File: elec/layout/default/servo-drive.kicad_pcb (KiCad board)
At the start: 4 copper layers, 37.6 x 39.9 mm, 125 parts

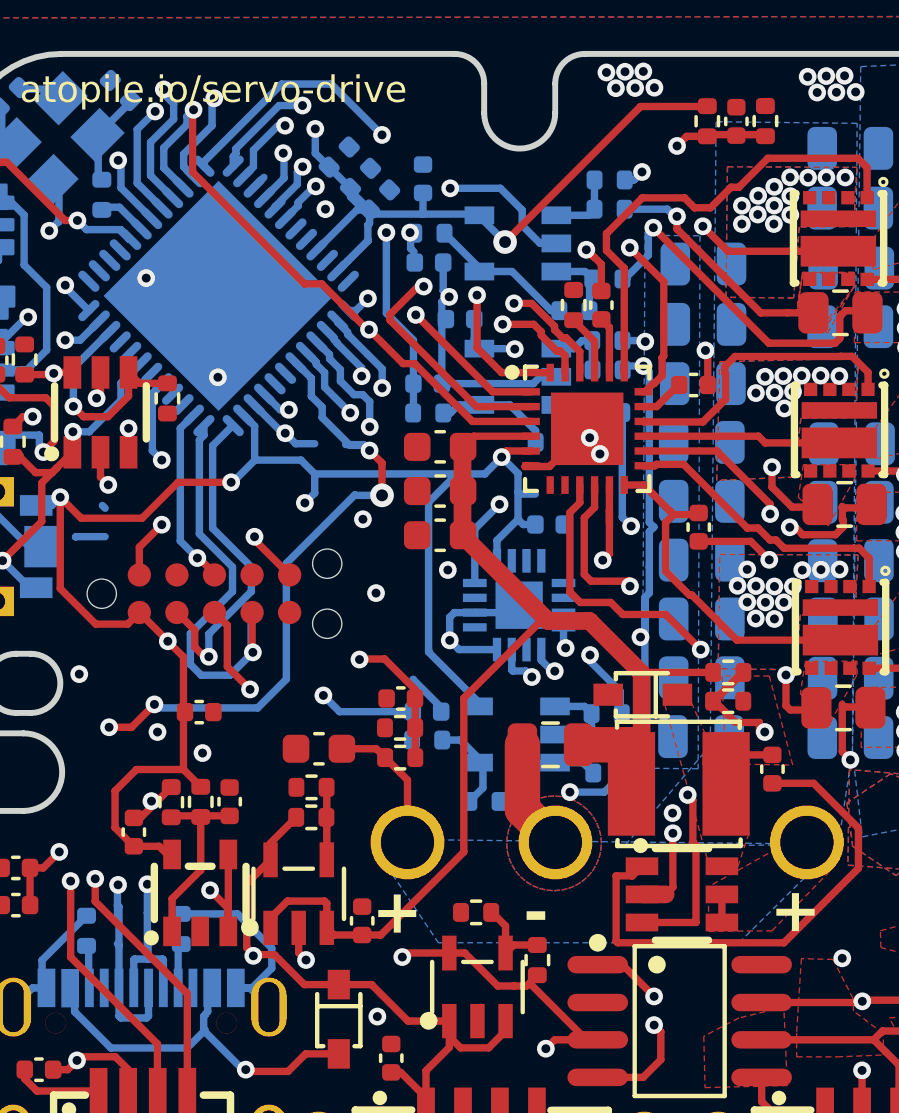
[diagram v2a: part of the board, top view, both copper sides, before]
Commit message: swapping MA732 for MT6835 sensor
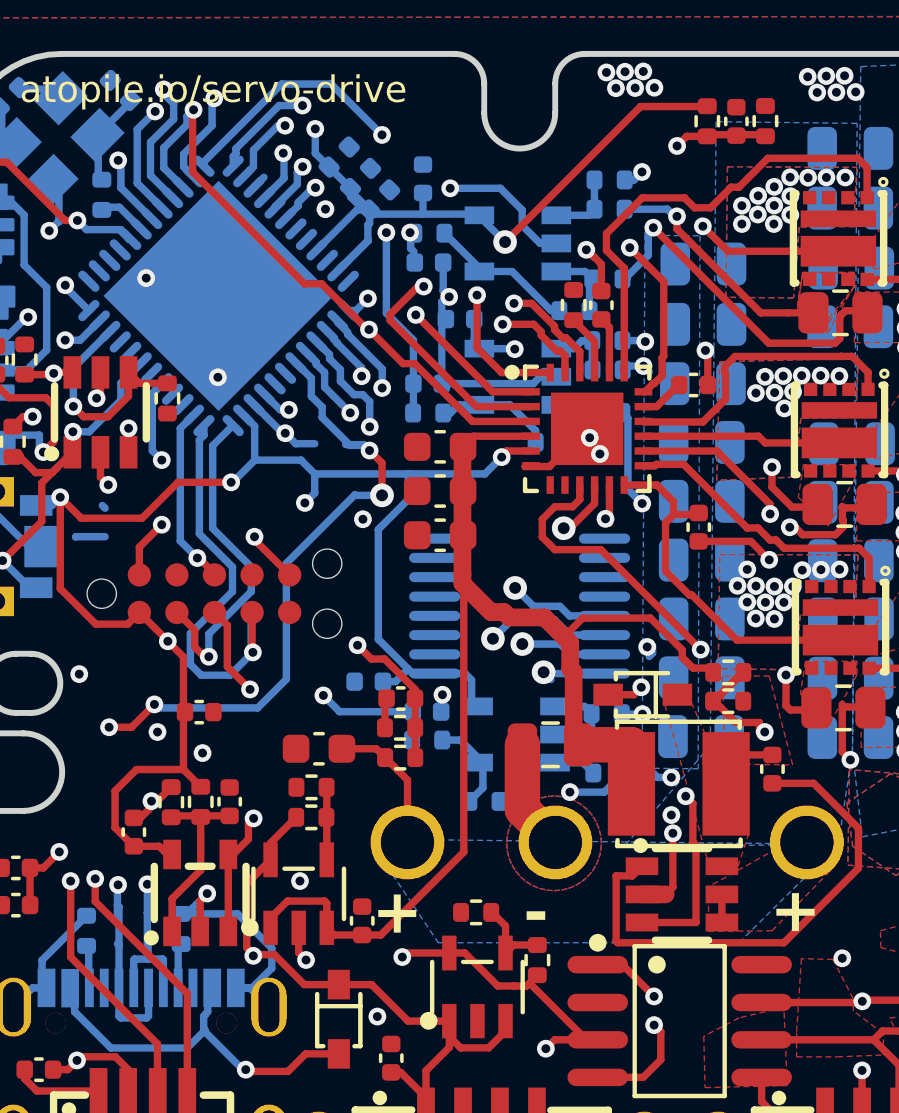
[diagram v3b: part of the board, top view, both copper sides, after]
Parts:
- removed the C1 at (224.7, 97.6)
- removed the U18 at (223.7, 100.4)
- added C18: 16V 100nF X7R ±10% 0402 Multilayer Ceramic Capacitors MLCC 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, lib:C0402, B.Cu at (218.6, 102.9)
- added U29: , lib:TSSOP-16_L5.0-W4.4-P0.65-LS6.4-BL, B.Cu at (223.7, 100.4)
- C24: value 16V 220nF X7R ±10% 0402 Multilayer Ceramic Capacitors MLCC - SMD/SMT ROHS -> 16V 100nF X7R ±10% 0402 Multilayer Ceramic Capacitors MLCC - SMD/SMT ROHS
- C42, C44: value 50V 20pF C0G ±5% 0402 Multilayer Ceramic Capacitors MLCC - SMD/SMT ROHS -> 50V 18pF C0G ±5% 0402 Multilayer Ceramic Capacitors MLCC - SMD/SMT ROHS
- R1, R15, R20, R38: value 62.5mW Thick Film Resistors ±100ppm/℃ ±1% 10kΩ 0402 Chip Resistor - Surface Mount ROHS -> 62.5mW Thick Film Resistors 50V ±100ppm/℃ ±1% 10kΩ 0402 Chip Resistor - Surface Mount ROHS
- R10: value 62.5mW Thick Film Resistors ±100ppm/℃ ±1% 27.4kΩ 0402 Chip Resistor - Surface Mount ROHS -> 62.5mW Thick Film Resistors 50V ±100ppm/℃ ±0.5% 27.4kΩ 0402 Chip Resistor - Surface Mount ROHS
- R11: value 62.5mW ±1% ±200ppm/℃ 3.01kΩ 0402 Chip Resistor - Surface Mount ROHS -> 62.5mW Thick Film Resistors 50V ±100ppm/℃ ±1% 3kΩ 0402 Chip Resistor - Surface Mount ROHS
- R12, R14, R26, R45, R49, R51: value 62.5mW Thick Film Resistors ±100ppm/℃ ±1% 47kΩ 0402 Chip Resistor - Surface Mount ROHS -> 62.5mW Thick Film Resistors 50V ±100ppm/℃ ±1% 47kΩ 0402 Chip Resistor - Surface Mount ROHS
- R13, R2, R25, R44, R48, R50, R6: value 62.5mW Thick Film Resistors ±100ppm/℃ ±1% 1kΩ 0402 Chip Resistor - Surface Mount ROHS -> 62.5mW Thick Film Resistors 50V ±100ppm/℃ ±1% 1kΩ 0402 Chip Resistor - Surface Mount ROHS
- R16, R46, R52: value 62.5mW ±1% ±200ppm/℃ 73.2Ω 0402 Chip Resistor - Surface Mount ROHS -> 62.5mW Thick Film Resistors 50V ±100ppm/℃ ±1% 73.2Ω 0402 Chip Resistor - Surface Mount ROHS
- R17: value 62.5mW Thick Film Resistors ±100ppm/℃ ±1% 20.5kΩ 0402 Chip Resistor - Surface Mount ROHS -> 62.5mW Thick Film Resistors 50V ±100ppm/℃ ±1% 20.5kΩ 0402 Chip Resistor - Surface Mount ROHS
- R18: value 62.5mW Thick Film Resistors ±100ppm/℃ ±1% 6.34kΩ 0402 Chip Resistor - Surface Mount ROHS -> 62.5mW Thick Film Resistors 50V ±100ppm/℃ ±1% 6.34kΩ 0402 Chip Resistor - Surface Mount ROHS
- R19: value 10 +/- 0.1 (1%) kiloohm -> 10kohm +/- 1%
- R21: value 62.5mW Thick Film Resistors ±100ppm/℃ ±1% 11.5kΩ 0402 Chip Resistor - Surface Mount ROHS -> 62.5mW Thick Film Resistors 50V ±100ppm/℃ ±1% 11.5kΩ 0402 Chip Resistor - Surface Mount ROHS
- R22: value 62.5mW Thick Film Resistors ±100ppm/℃ ±1% 6.19kΩ 0402 Chip Resistor - Surface Mount ROHS -> 62.5mW Thick Film Resistors 50V ±100ppm/℃ ±1% 6.2kΩ 0402 Chip Resistor - Surface Mount ROHS
- R29: value 62.5mW Thick Film Resistors ±100ppm/℃ ±1% 41.2kΩ 0402 Chip Resistor - Surface Mount ROHS -> 62.5mW Thick Film Resistors 50V ±100ppm/℃ ±1% 41.2kΩ 0402 Chip Resistor - Surface Mount ROHS
- R3: value 62.5mW Thick Film Resistors ±100ppm/℃ ±1% 100kΩ 0402 Chip Resistor - Surface Mount ROHS -> 62.5mW Thick Film Resistors 50V ±100ppm/℃ ±1% 100kΩ 0402 Chip Resistor - Surface Mount ROHS
- R30: value 62.5mW Thick Film Resistors ±100ppm/℃ ±1% 4.32kΩ 0402 Chip Resistor - Surface Mount ROHS -> 62.5mW Thick Film Resistors 50V ±100ppm/℃ ±1% 4.3kΩ 0402 Chip Resistor - Surface Mount ROHS
- R31: value 62.5mW Thick Film Resistors ±100ppm/℃ ±1% 40.2kΩ 0402 Chip Resistor - Surface Mount ROHS -> 62.5mW Thick Film Resistors 50V ±100ppm/℃ ±1% 41.2kΩ 0402 Chip Resistor - Surface Mount ROHS
- R5, R9: value 62.5mW Thick Film Resistors ±100ppm/℃ ±1% 5.1kΩ 0402 Chip Resistor - Surface Mount ROHS -> 62.5mW Thick Film Resistors 50V ±100ppm/℃ ±1% 5.1kΩ 0402 Chip Resistor - Surface Mount ROHS
- R7: value 62.5mW Thick Film Resistors ±100ppm/℃ ±1% 220Ω 0402 Chip Resistor - Surface Mount ROHS -> 62.5mW Thick Film Resistors 50V ±100ppm/℃ ±1% 220Ω 0402 Chip Resistor - Surface Mount ROHS
- renumbered C9 to C1, C15 to C14, C16 to C15, C18 to C16, C14 to C9, U29 to U18
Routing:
- net sck: track 11.5 -> 17.0 mm
- net power_stage.phase_c.current_sensor.bias_div-vcc: track 11.0 -> 7.42 mm
- net power_stage.phase_a.half_bridge-vcc-1: track 29.1 -> 26.0 mm
- net power_stage-vcc-1: track 41.4 -> 44.1 mm
- net power_stage-vcc-2: track 111.3 -> 108.8 mm, vias 15 -> 14
- net micro-mosi: track 19.3 -> 17.3 mm
- net power_stage.phase_b.half_bridge-vcc-1: track 19.4 -> 17.6 mm
- net power_stage-gnd: track 56.3 -> 54.7 mm, vias 88 -> 91
- net micro-miso: track 16.0 -> 14.7 mm
- net cs: track 17.6 -> 18.8 mm
- net power_stage.phase_b.current_sensor.feedback_div-vcc: track 12.2 -> 11.6 mm
- net power_stage.phase_c.half_bridge-vcc-1: track 18.5 -> 19.1 mm
- net power_stage.phase_a.current_sensor-vcc: track 47.1 -> 47.6 mm, vias 4 -> 5
- net (no net): vias 11 -> 10
